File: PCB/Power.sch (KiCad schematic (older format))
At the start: 17 parts, among them J10 FAN_2, J31 FAN_1, J33 V Motor In, Q7 Q_PMOS_DGS, U1 LM2678

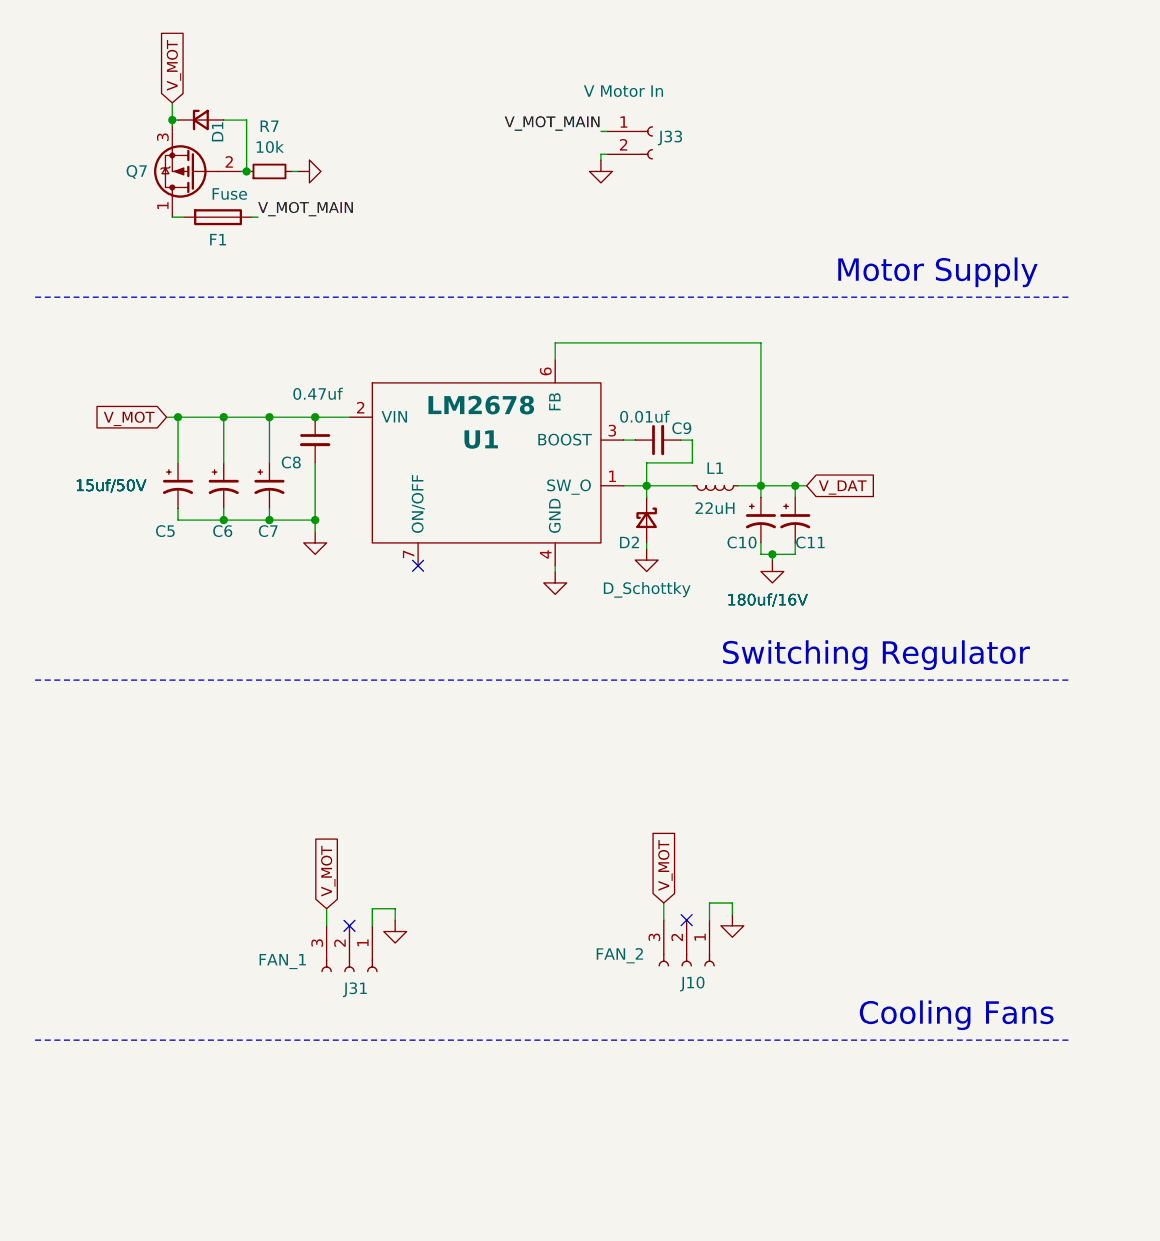
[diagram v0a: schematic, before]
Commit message: TOS new version
-Added usb power for display.
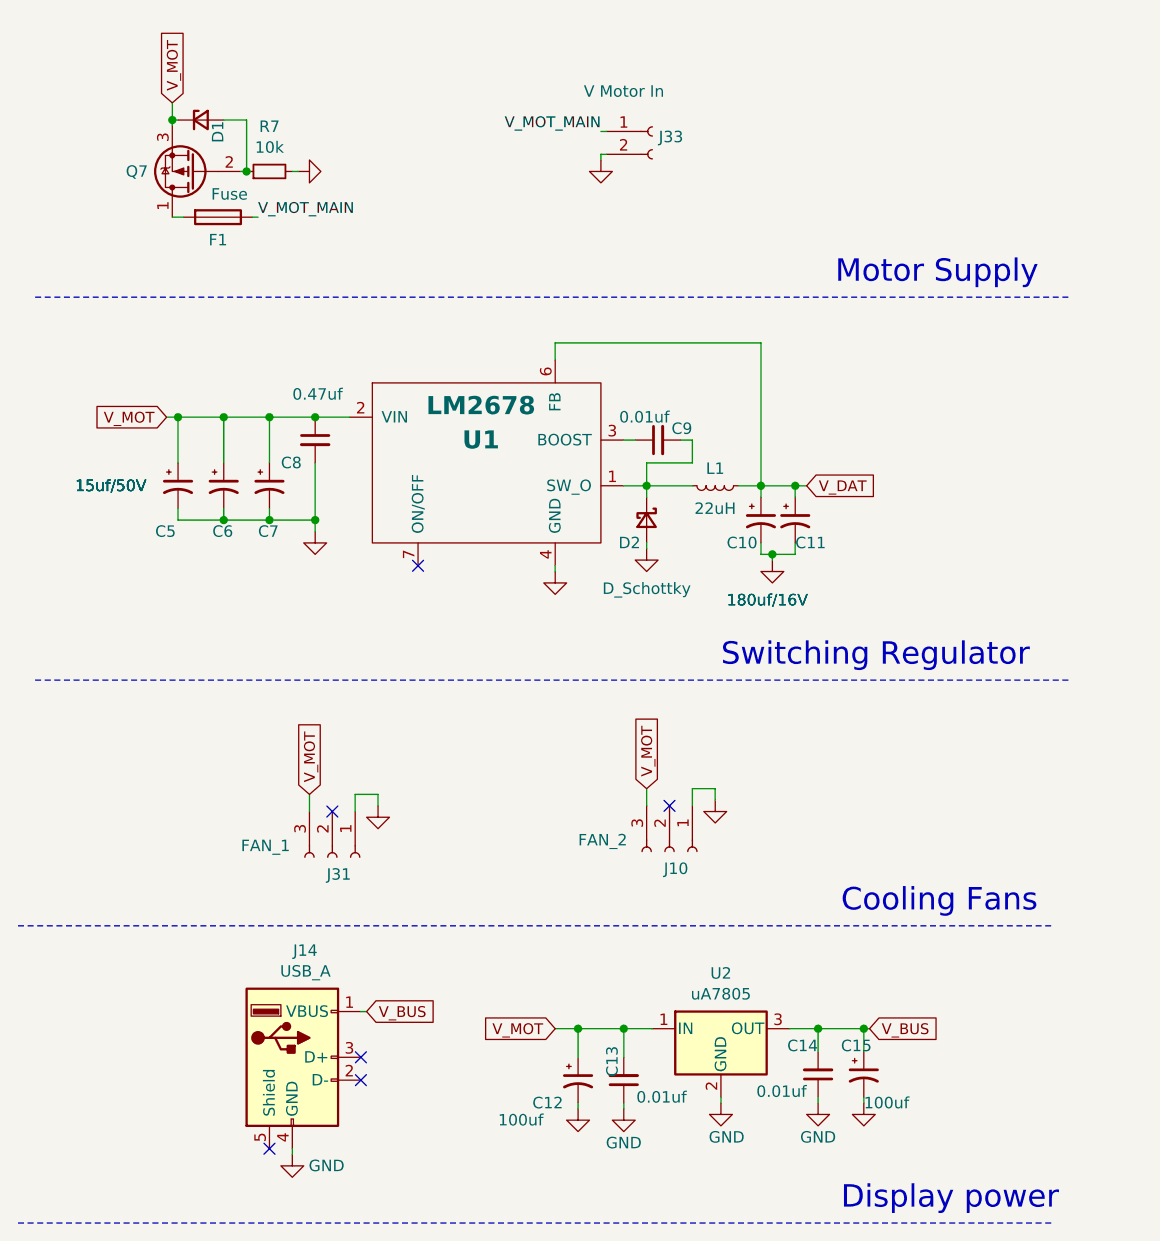
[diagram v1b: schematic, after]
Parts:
- added C12, C15: 100uf, Capacitor_SMD:CP_Elec_6.3x7.7, symbol Device:CP1_Small
- added C13, C14: 0.01uf, Capacitor_SMD:C_0805_2012Metric_Pad1.18x1.45mm_HandSolder, symbol Device:C_Small
- added J14: USB_A, Connector_USB:USB_A_CNCTech_1001-011-01101_Horizontal, symbol Connector:USB_A
- added U2: uA7805, Package_TO_SOT_SMD:TO-263-3_TabPin2, symbol Regulator_Linear:uA7805
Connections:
- net GND: now also C12.2, C13.1, C14.1, C15.2, J14.4 (GND), U2.2 (GND)
- net V_MOT: now also C12.1, C13.2, U2.1 (IN)
- new net V_BUS: C14.2, C15.1, J14.1 (VBUS), U2.3 (OUT)
- no-connect marks 3 -> 6
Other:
- note added: "Display power"
- moved on the sheet: J10, J31
